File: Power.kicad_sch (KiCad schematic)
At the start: 14 parts, among them Q3 BSN20, Q4 BSN20, U10 MCP1703Ax-330xxDB, U12 LTC4365TS8

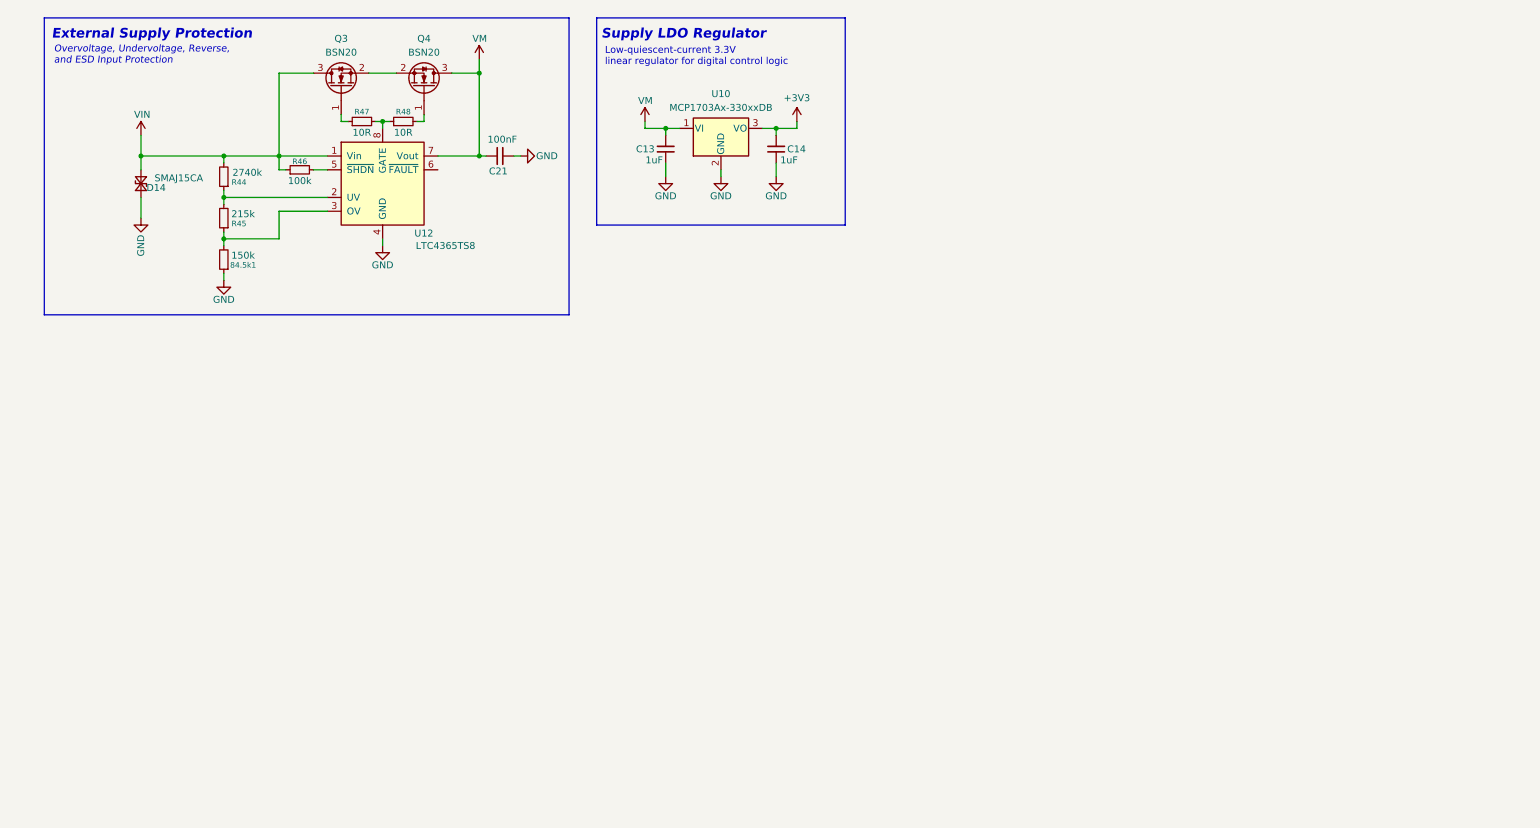
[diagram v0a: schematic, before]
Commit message: feat: add LTC4365 protection circuit and 3.3V logic LDO
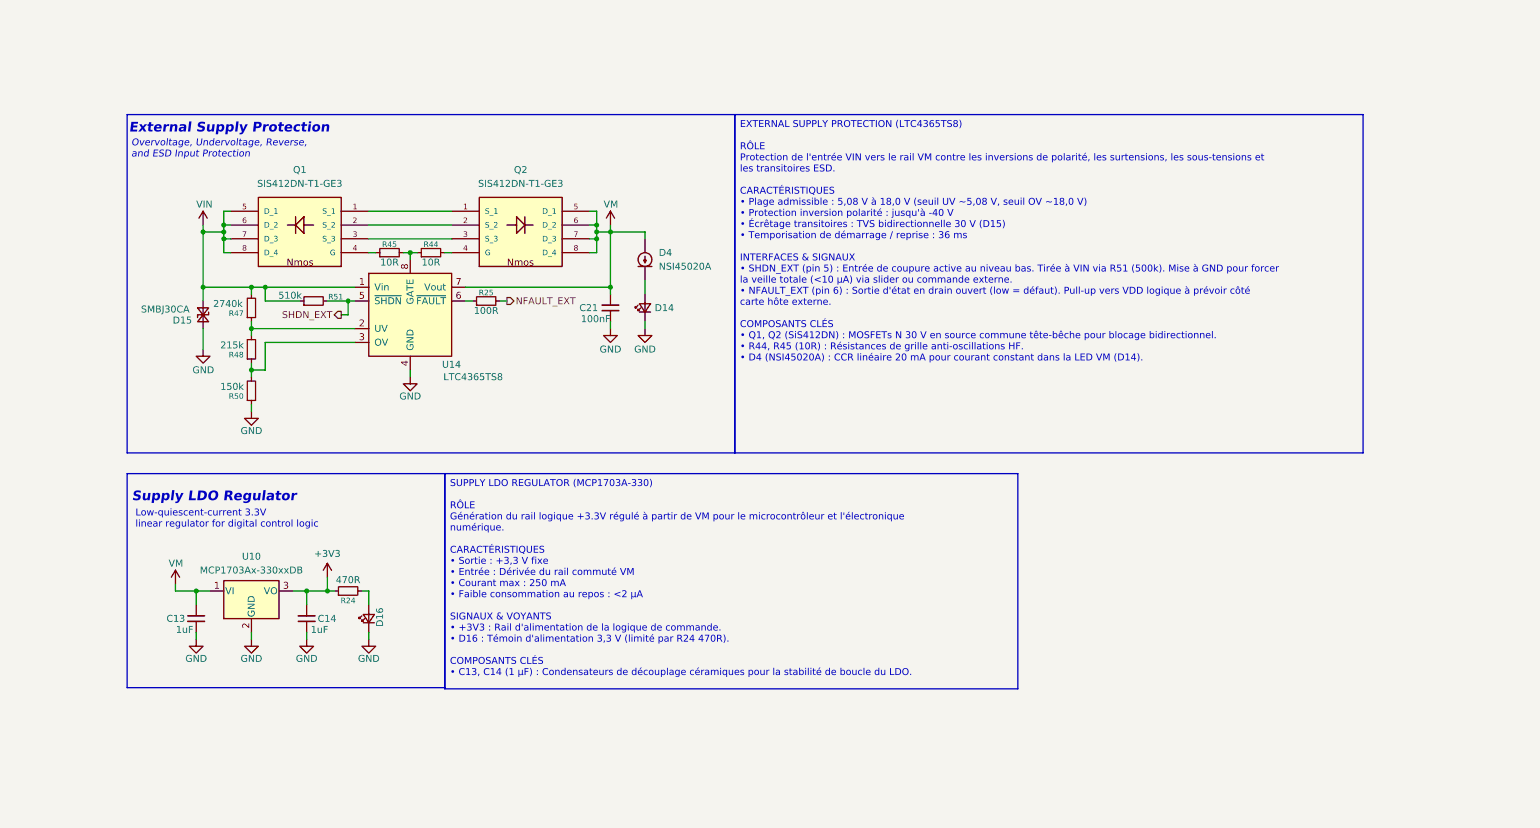
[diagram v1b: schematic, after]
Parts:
- removed 84.5k1: 150k, Resistor_SMD:R_0603_1608Metric, symbol Device:R_Small
- removed D14: SMAJ15CA, Diode_SMD:D_SMA, symbol Device:D_TVS_Small
- removed Q3, Q4: BSN20, Package_TO_SOT_SMD:SOT-23, symbol Transistor_FET:BSN20
- removed R46: 100k, Resistor_SMD:R_0603_1608Metric, symbol Device:R_Small
- removed U12: LTC4365TS8, Package_TO_SOT_SMD:TSOT-23-8, symbol Power_Management:LTC4365TS8
- added D14, D16: LED_Small, LED_SMD:LED_0603_1608Metric, symbol Device:LED_Small
- added D15: SMBJ30CA, Diode_SMD:D_SMA, symbol Device:D_TVS_Small
- added D4: NSI45020A, Diode_SMD:D_SOD-123, symbol Device:D_Current-regulator
- added Q1, Q2: SIS412DN-T1-GE3, SIS412DN-T1-GE3:POWERPAK-1212-8, symbol KineticCore:SIS412DN-T1-GE3
- added R24: 470R, Resistor_SMD:R_0603_1608Metric, symbol Device:R_Small
- added R25: 100R, Resistor_SMD:R_0603_1608Metric, symbol Device:R_Small
- added R50: 150k, Resistor_SMD:R_0603_1608Metric, symbol Device:R_Small
- added R51: 510k, Resistor_SMD:R_0603_1608Metric, symbol Device:R_Small
- added U14: LTC4365TS8, Package_TO_SOT_SMD:TSOT-23-8, symbol Power_Management:LTC4365TS8
- R44: value 2740k -> 10R
- R45: value 215k -> 10R
- R47: value 10R -> 2740k
- R48: value 10R -> 215k
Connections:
- net +3V3: now also R24.1
- net GND: now also D14.1 (K), D15.2 (A2), D16.1 (K), R50.1, U14.4 (GND)
- net VIN: now also R47.2, D15.1 (A1), Q1.5 (D_1), Q1.6 (D_2), Q1.7 (D_3), Q1.8 (D_4), R51.1, U14.1 (Vin); no longer R44.2
- net VM: now also D4.2 (A), Q2.5 (D_1), Q2.6 (D_2), Q2.7 (D_3), Q2.8 (D_4), U14.7 (Vout)
- net at R47.1: now also R48.2, U14.2 (UV)
- net at R45.1: now also Q1.4 (G)
- net at R44.1, R45.2: now also U14.8 (GATE)
- net at R48.1: now also R50.2, U14.3 (OV); no longer R47.2
- new net: D14.2 (A), D4.1 (K)
- new net: D16.2 (A), R24.2
- new net: Q2.4 (G), R44.2
- new net: Q1.1 (S_1), Q2.1 (S_1)
- new net: Q1.2 (S_2), Q2.2 (S_2)
- new net: Q1.3 (S_3), Q2.3 (S_3)
- new net: R25.1, U14.6 (~{FAULT})
- new net NFAULT_EXT: R25.2
- new net SHDN_EXT: R51.2, U14.5 (~{SHDN})
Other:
- moved on the sheet: C13, C14, U10

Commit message: feat: add standardized functional notes across all schematic sheets
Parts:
- added SW2: OS102011MA1Q, Button_Switch_THT:SW_Slide_SPDT_Angled_CK_OS102011MA1Q, symbol Switch:SW_SPDT
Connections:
- net GND: now also SW2.3 (C)
- net SHDN_EXT: now also SW2.2 (B)
- no-connect marks 0 -> 1
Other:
- note added: "Manual Power Enable"
- note added: "On-board SPDT slide switch for manual power shutdown and sleep mode (< 10 µA)."
- company: (none) -> BerryRocket
- title: (none) -> KinetiCoreDC - Power 
- moved on the sheet: C13, C14, D14, D16, D4, R24, U10

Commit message: fix: fix some errors in shematic
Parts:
- removed SW2: OS102011MA1Q, Button_Switch_THT:SW_Slide_SPDT_Angled_CK_OS102011MA1Q, symbol Switch:SW_SPDT
- Q1, Q2: footprint SIS412DN-T1-GE3:POWERPAK-1212-8 -> KineticCore:POWERPAK-1212-8
- R44: renamed from R47; value 2740k -> 2.7M
- R45: renamed from R48; value 215k -> 150k
- R46: renamed from R50; value 150k -> 100k
- renumbered C13 to C24, C14 to C25, C21 to C26, D15 to D12, D16 to D13, D4 to D14, D14 to D15, R51 to R47, R24 to R48, R45 to R49, R44 to R50, R25 to R51, U10 to U11, U14 to U12
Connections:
- net at Q1.1 (S_1), Q2.1 (S_1): now also Q1.2 (S_2), Q1.3 (S_3), Q2.2 (S_2), Q2.3 (S_3)
- no-connect marks 1 -> 0
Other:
- note removed: "Manual Power Enable"
- note removed: "On-board SPDT slide switch for manual power shutdown and sleep mode (< 10 µA)."
- moved on the sheet: C24, C25, C26, D12, D13, D14, D15, Q1, Q2, R44, R45, R46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

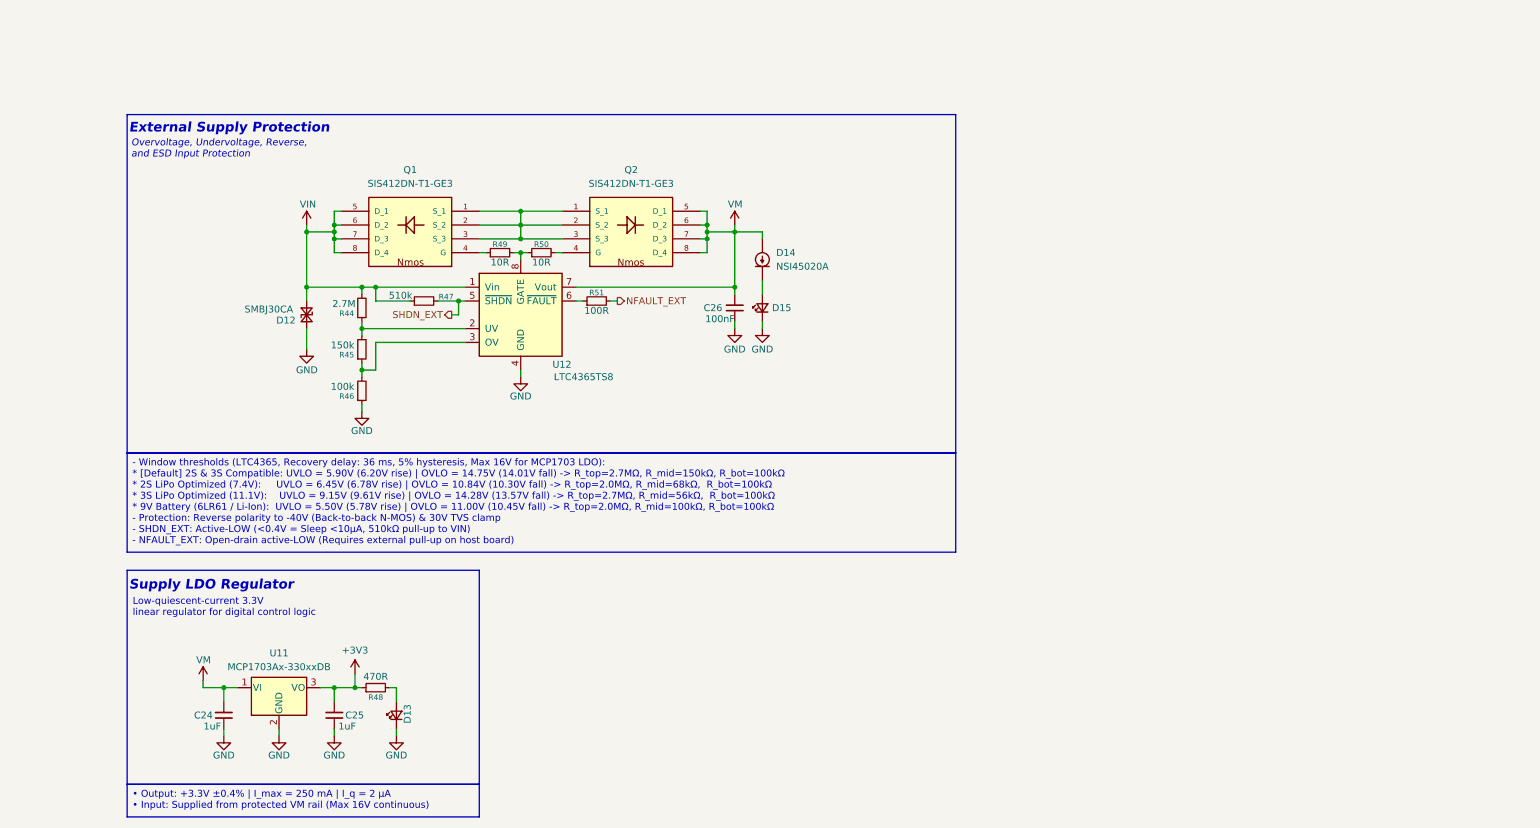
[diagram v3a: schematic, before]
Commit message: wip(sch): draft JST-XH and solder pad connector interfaces
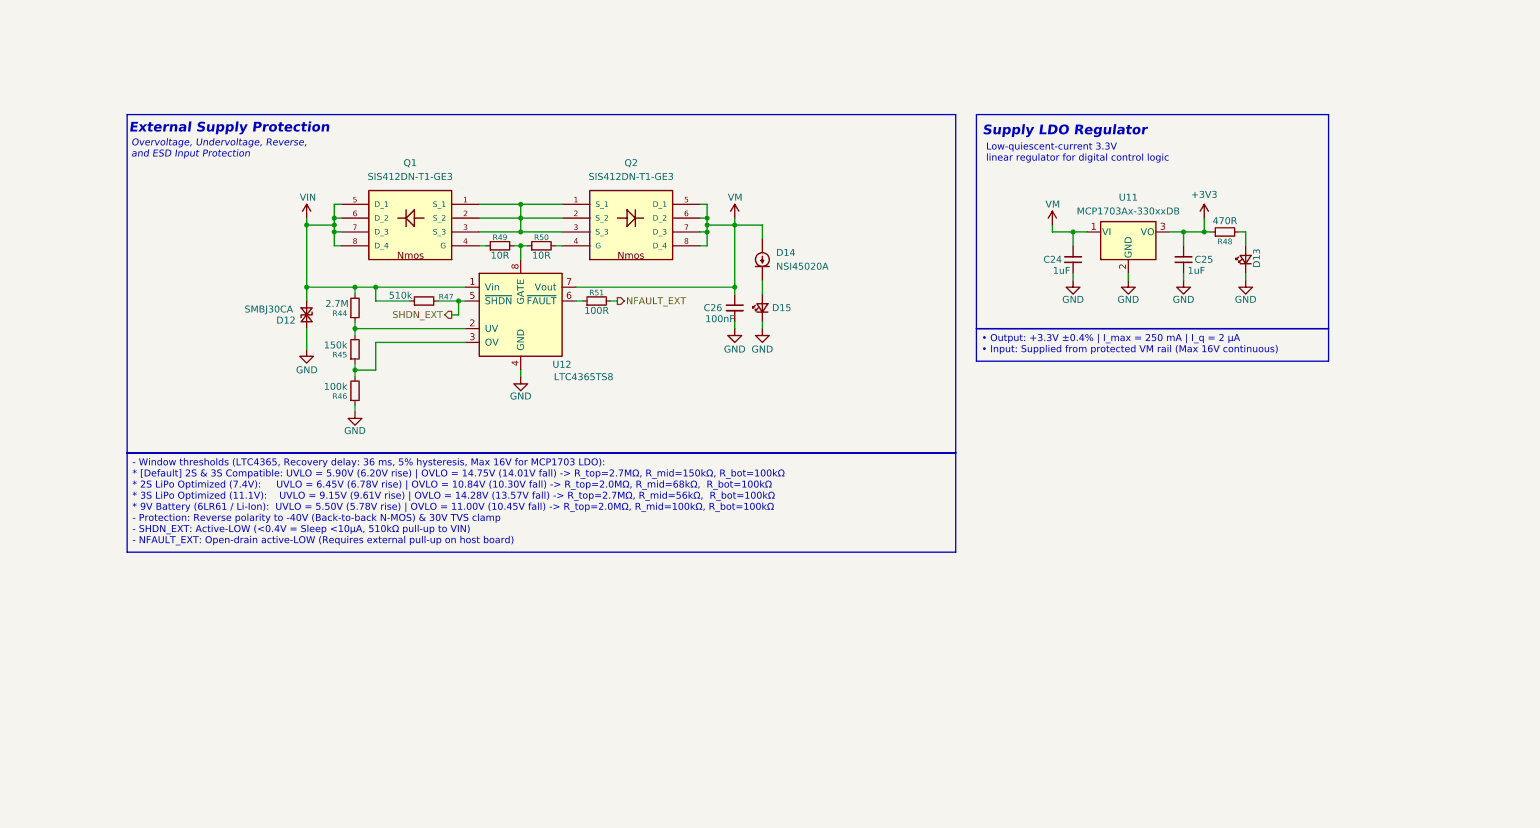
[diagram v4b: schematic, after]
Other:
- moved on the sheet: C24, C25, D13, Q1, Q2, R44, R45, R46, R48, R49, R50, U11

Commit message: refactor(schematic): migrate MCU to LQFP48 and finalize pinout mapping
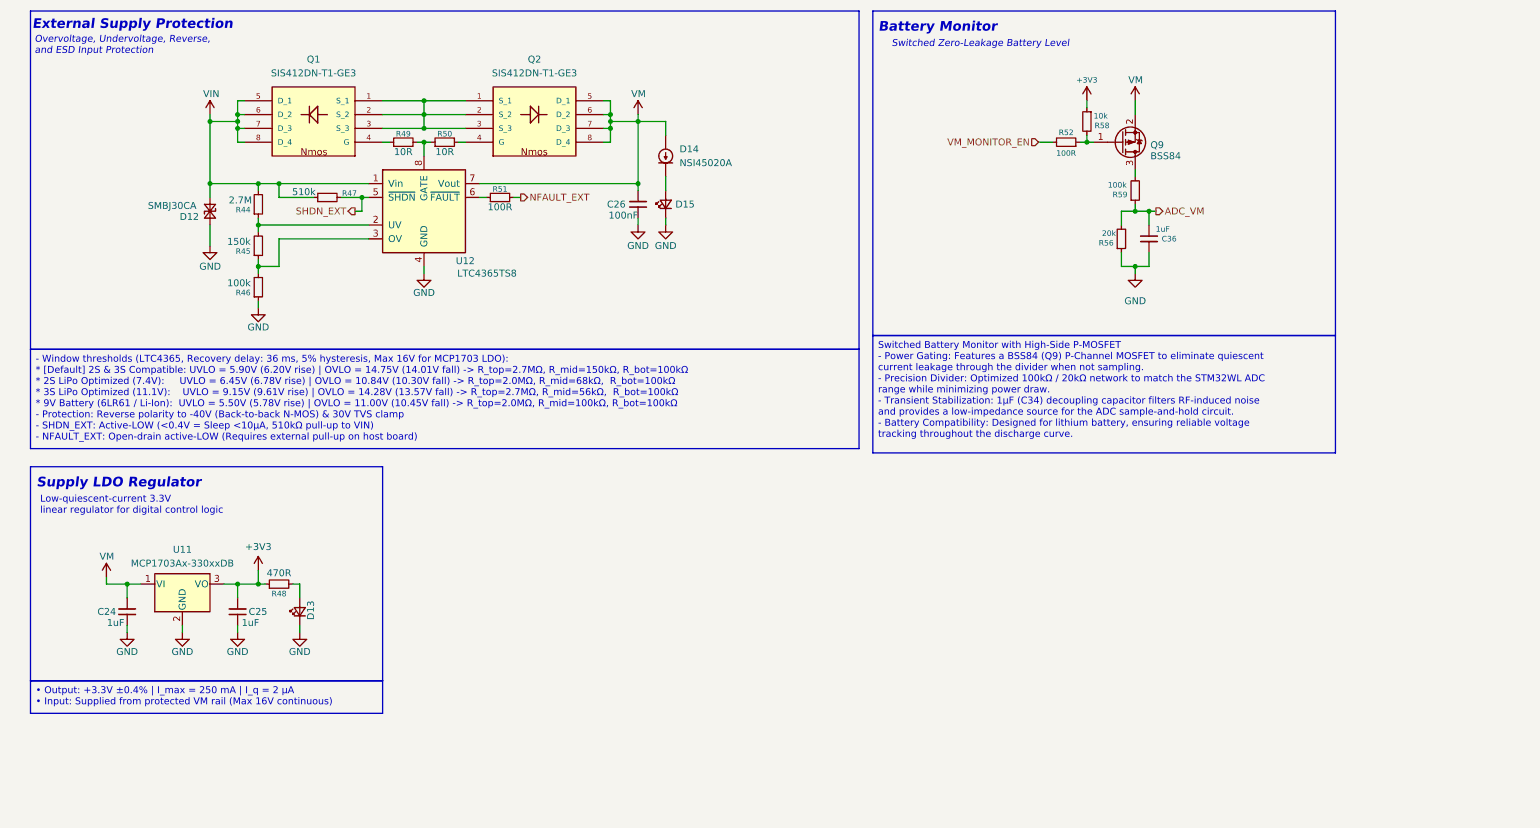
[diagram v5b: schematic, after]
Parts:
- added C36: 1uF, Capacitor_SMD:C_0603_1608Metric, symbol Device:C_Small
- added Q9: BSS84, Package_TO_SOT_SMD:SOT-23, symbol Transistor_FET:BSS84
- added R52: 100R, Resistor_SMD:R_0603_1608Metric, symbol Device:R_Small
- added R56: 20k, Resistor_SMD:R_0603_1608Metric, symbol Device:R_Small
- added R58: 10k, Resistor_SMD:R_0603_1608Metric, symbol Device:R_Small
- added R59: 100k, Resistor_SMD:R_0603_1608Metric, symbol Device:R_Small
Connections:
- net +3V3: now also R58.1
- net GND: now also C36.1, R56.1
- net VM: now also Q9.2 (S)
- new net: Q9.1 (G), R52.1, R58.2
- new net: Q9.3 (D), R59.2
- new net ADC_VM: C36.2, R56.2, R59.1
- new net VM_MONITOR_EN: R52.2
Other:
- note added: "Battery Monitor"
- note added: "Switched Zero-Leakage Battery Level"
- moved on the sheet: C24, C25, C26, D12, D13, D14, D15, Q1, Q2, R44, R45, R46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

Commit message: feat : add SMLVN6RGB status LED stage with balanced 3.3V ballast resistors
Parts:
- added D18: SMLVN6RGB, LED_SMD:LED_ROHM_SMLVN6, symbol LED:SMLVN6RGB
- added R62: 330R, Resistor_SMD:R_0603_1608Metric, symbol Device:R_Small
- added R63, R82: 180R, Resistor_SMD:R_0603_1608Metric, symbol Device:R_Small
- D12: value SMBJ30CA -> SMBJ15CA
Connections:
- net +3V3: now also D18.1 (BA), D18.2 (RA), D18.3 (GA)
- new net: D18.4 (GK), R82.1
- new net: D18.5 (RK), R62.1
- new net: D18.6 (BK), R63.1
- new net BLUE_MCU: R63.2
- new net GREEN_MCU: R82.2
- new net RED_MCU: R62.2
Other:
- note added: "Low quiescent current 3.3V linear regulator for digital control logic"
- note added: "RGB Led Indicator"
- note added: "Status LED - Active-LOW Sink Control"
- note removed: "Low-quiescent-current 3.3V linear regulator for digital control logic"
- moved on the sheet: C24, C25, D13, R48, U11
